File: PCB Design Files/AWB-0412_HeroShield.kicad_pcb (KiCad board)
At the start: 2 copper layers, 68.6 x 53.3 mm, 25 parts, among them J1 Power, J2 Digital/PWM, J3 Analog, J4 Digital/PWM

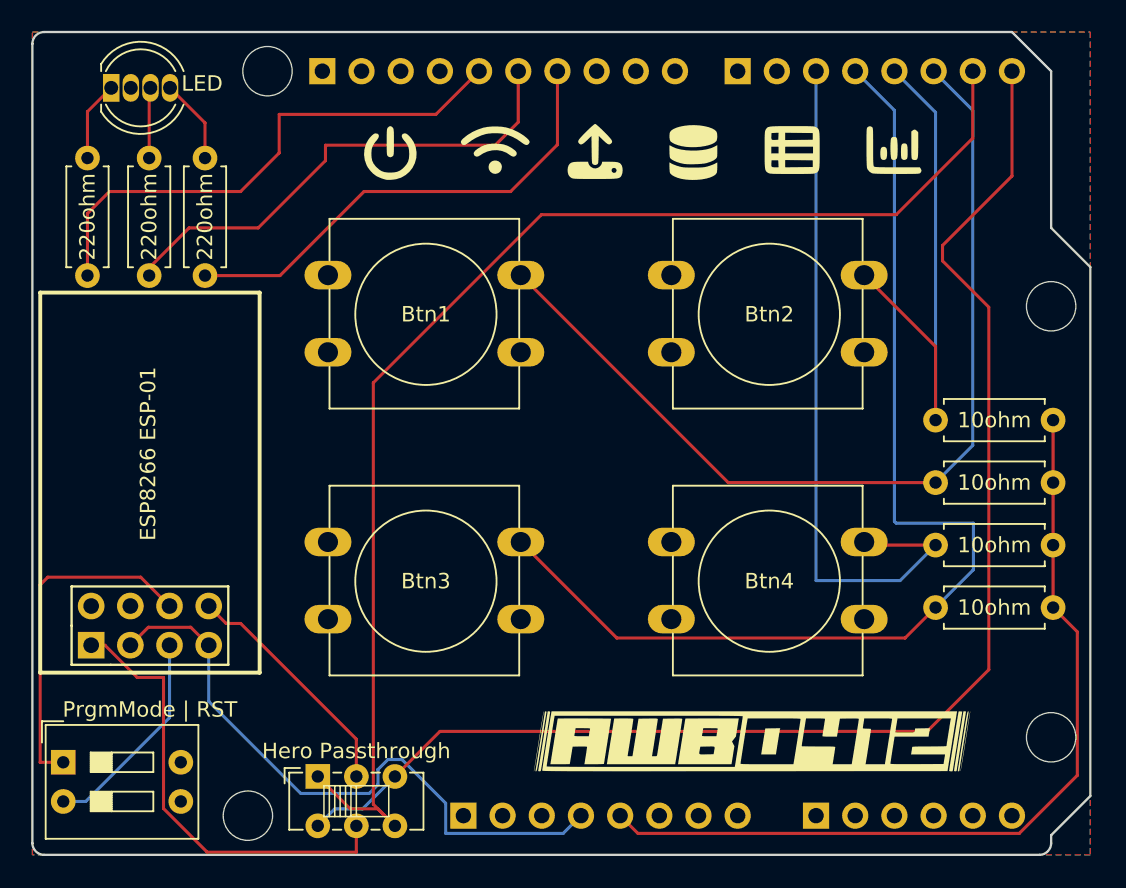
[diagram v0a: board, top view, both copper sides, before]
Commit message: Update PCB files
Updated the PCB files. Altered LED connections to ensure analog out compatible pins were connected to the LED. As well as added a JST PH 2-Pin connector for providing power.
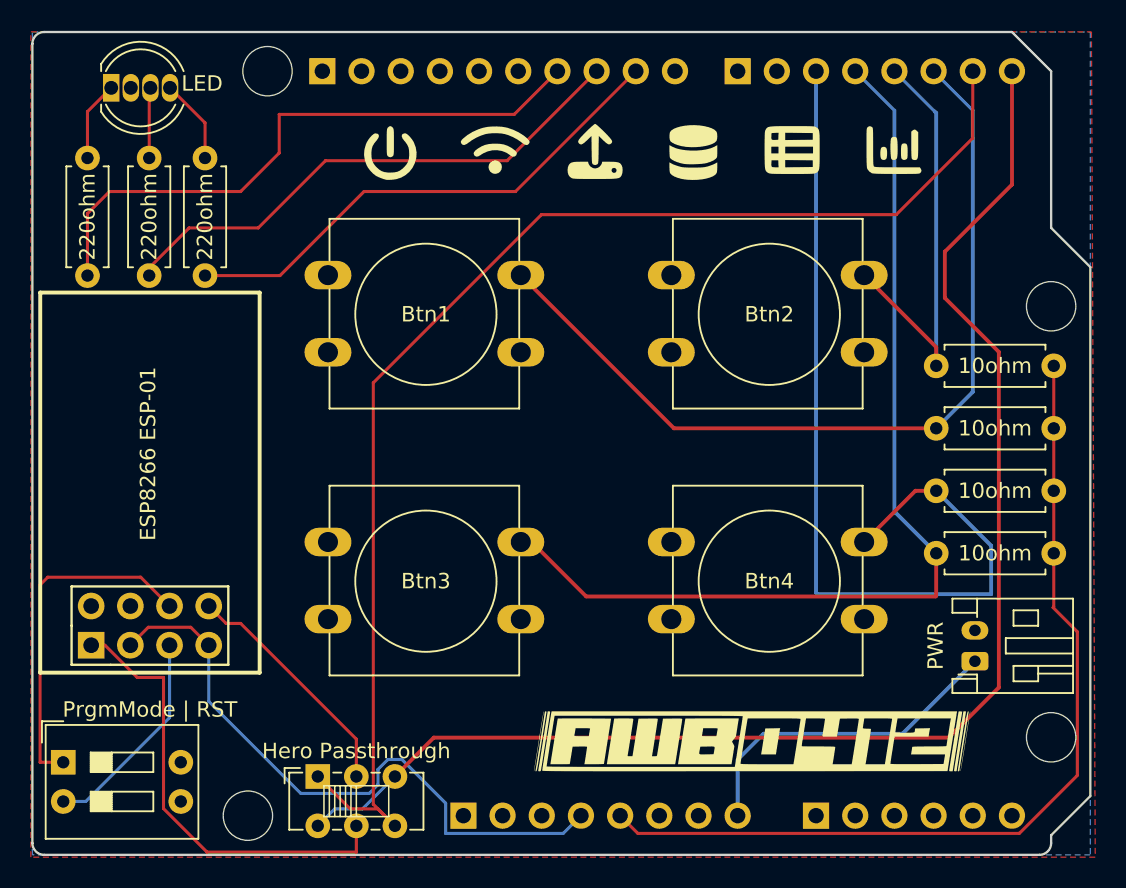
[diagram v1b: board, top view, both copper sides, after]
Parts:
- added PWR: JST_PH_S2B-PH-K_1x02_P2.00mm_Horizontal, Connector_JST:JST_PH_S2B-PH-K_1x02_P2.00mm_Horizontal, F.Cu at (161.1, 87.5)
- moved 10ohm 3.52 mm to (158.6, 72.3)
- moved 10ohm 3.52 mm to (158.6, 80.5)
- moved 10ohm 3.52 mm to (158.6, 68.3)
- moved 10ohm 3.52 mm to (158.6, 76.4)
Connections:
- 220ohm pad 1: /12 -> /*10
- 220ohm pad 1: /13 -> /*11
- 220ohm pad 1: /*11 -> /*9
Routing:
- net /*10: track 0.00 -> 35.0 mm
- net /13: track 34.7 -> 0.00 mm
- net /*9: track 0.00 -> 33.4 mm
- net /12: track 32.5 -> 0.00 mm
- net VCC: track 0.00 -> 21.7 mm
- net /*5: track 46.5 -> 59.7 mm
- net /*11: track 31.1 -> 39.8 mm
- net /4: track 72.2 -> 64.8 mm
- net /*3: track 35.0 -> 28.1 mm
- net /2: track 61.2 -> 56.2 mm
- net +5V: track 55.4 -> 58.9 mm
- net /RX/0: track 89.6 -> 91.1 mm
